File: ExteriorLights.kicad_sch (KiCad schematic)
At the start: 32 parts, among them J1 Left_Signal, J2 Right_Signal, J29 Headlight, J3 Brake Light, J4 Headlight, U1 EL3H7, U2 EL3H7, U3 EL3H7, U4 EL3H7

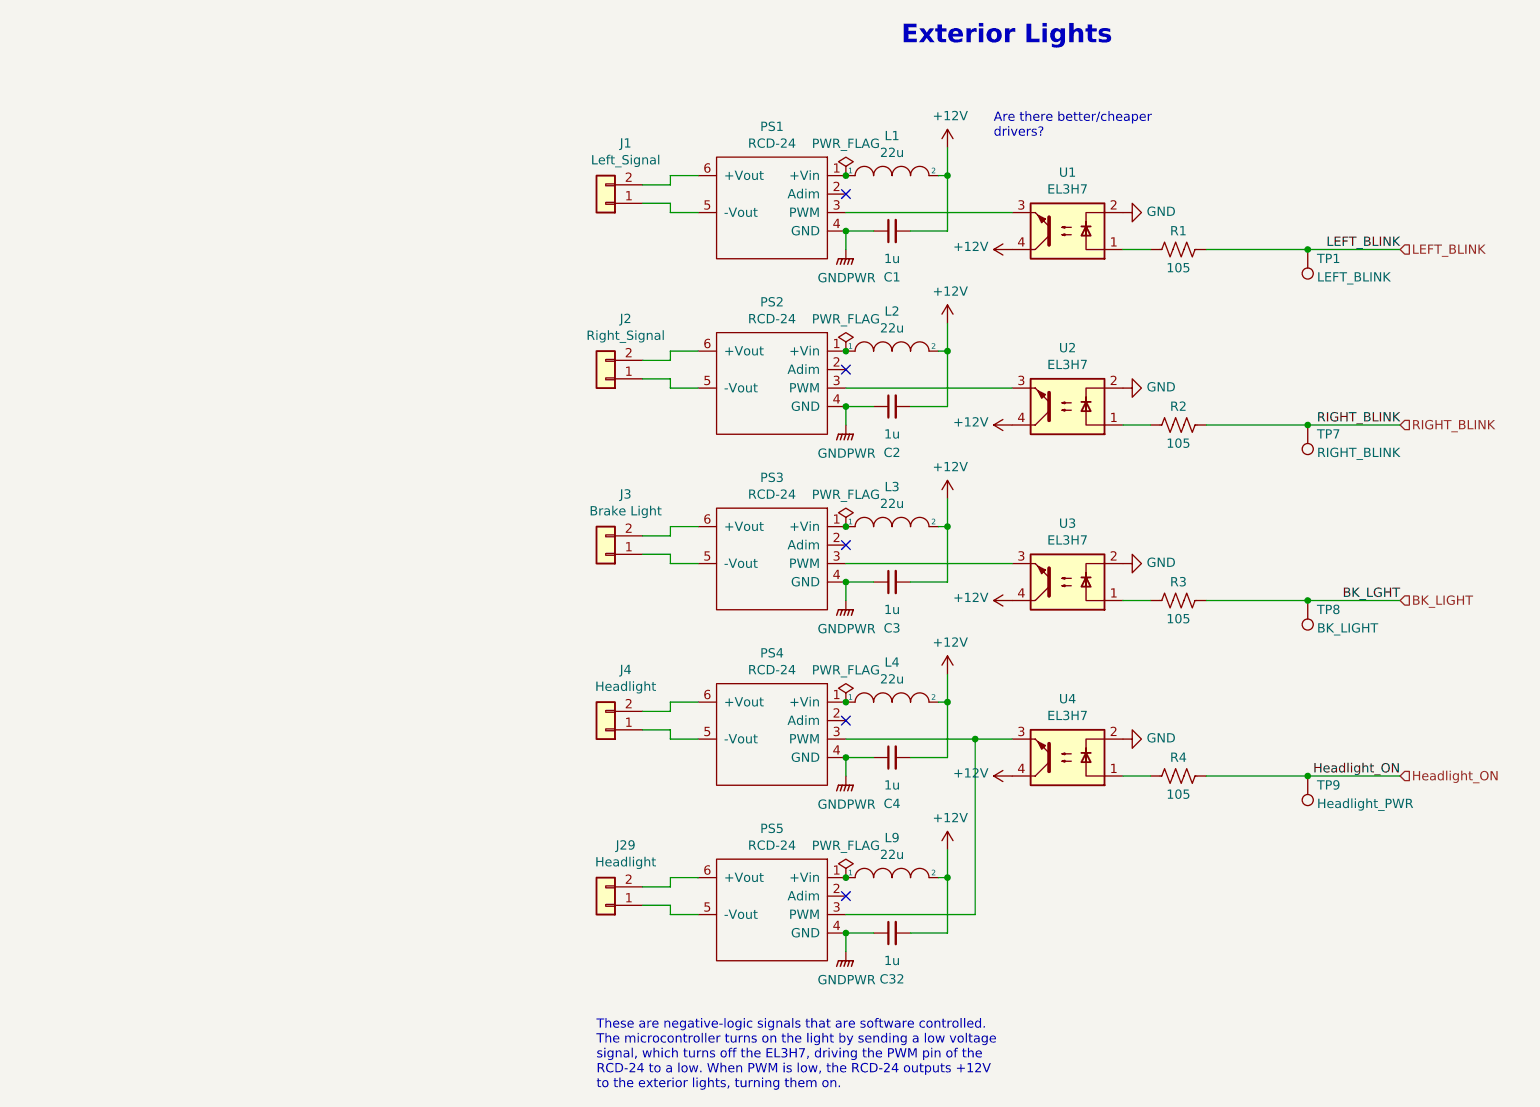
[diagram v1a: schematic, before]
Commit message: Schematic notations for rework changes
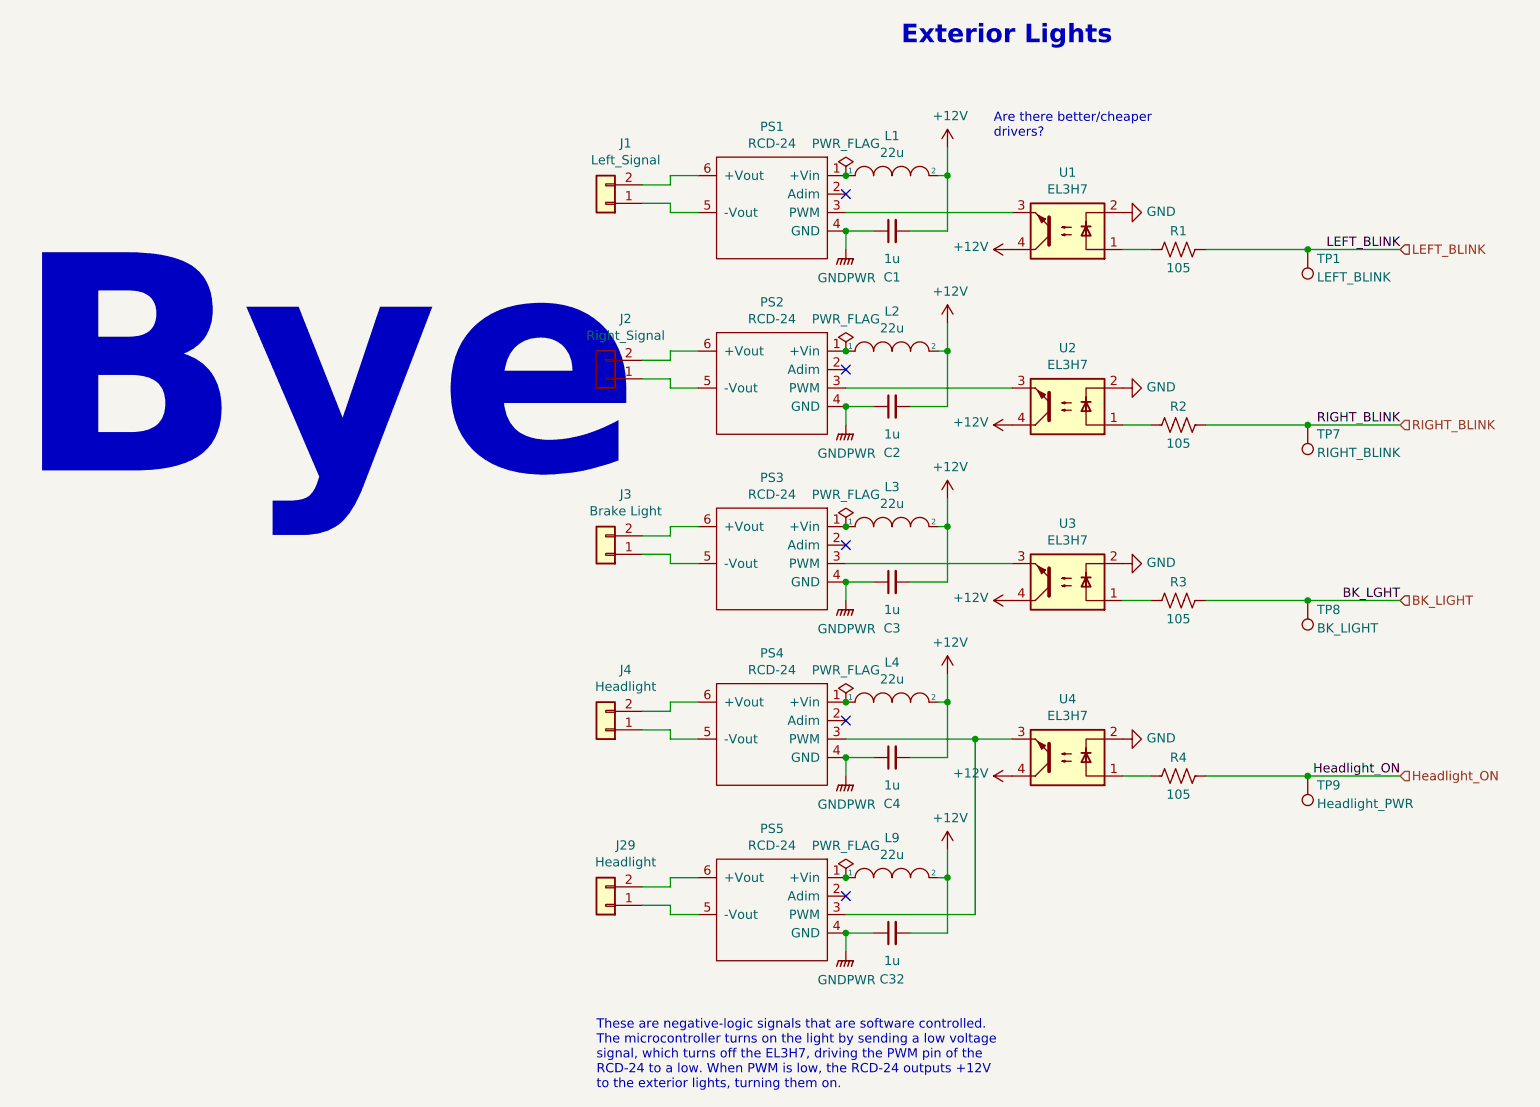
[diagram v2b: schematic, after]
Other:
- note added: "Bye"
